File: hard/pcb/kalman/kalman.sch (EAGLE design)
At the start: 89 parts, among them X1 USB-SMD-NS

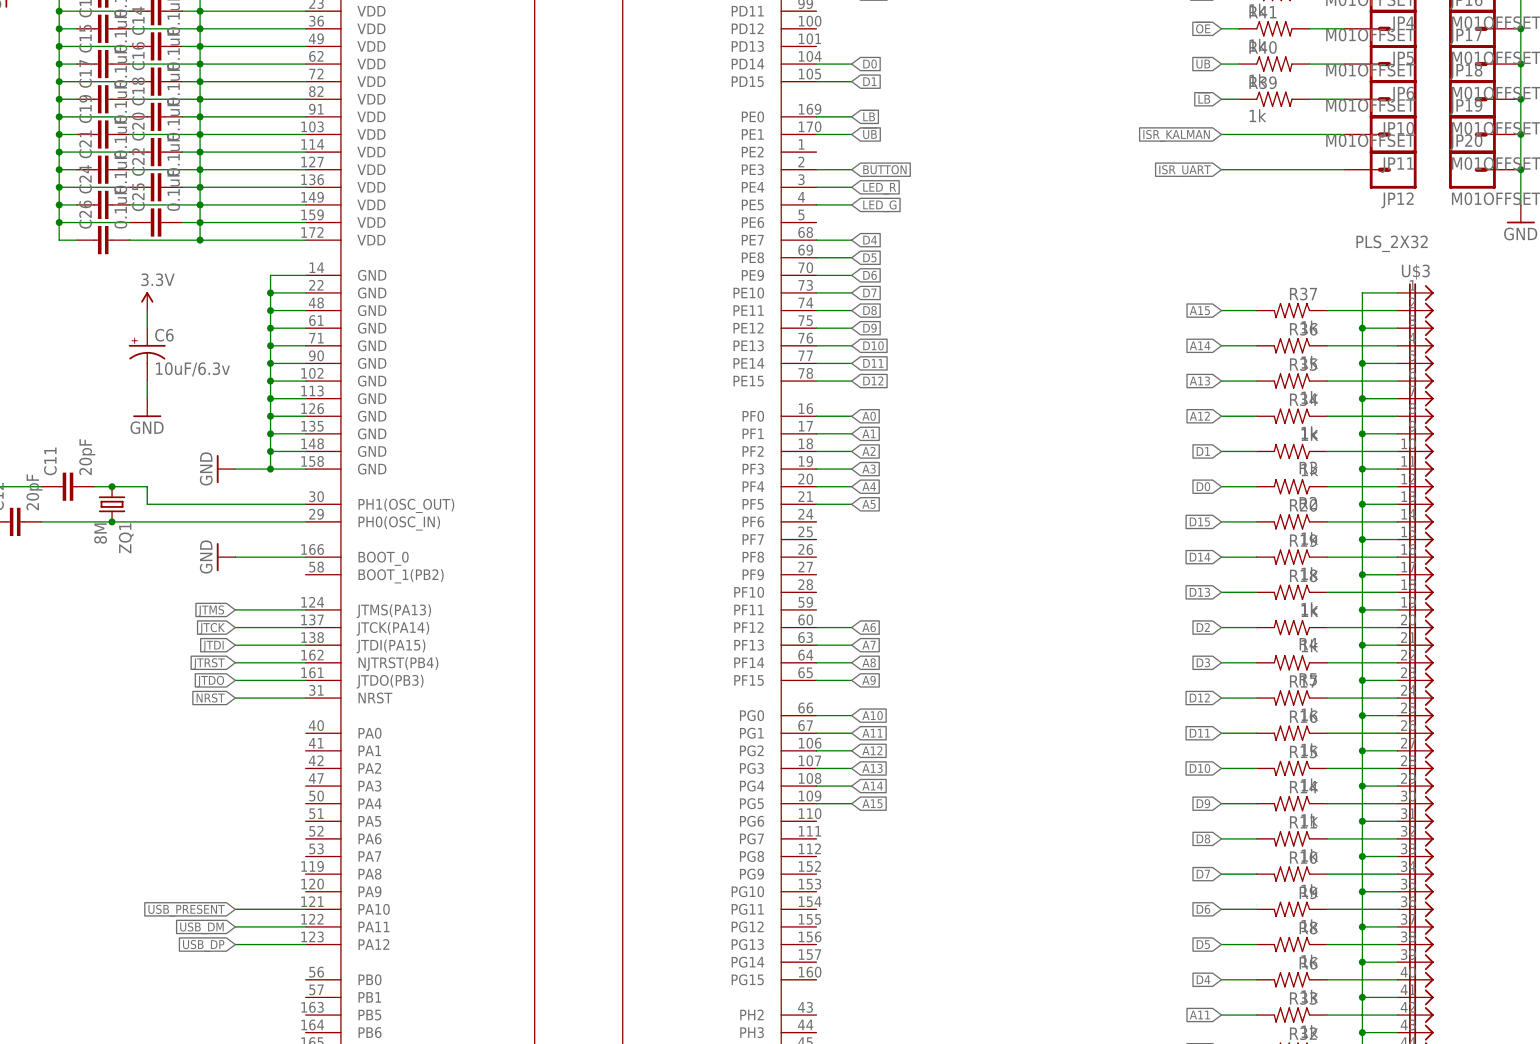
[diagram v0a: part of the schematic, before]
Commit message: updated kalman tester
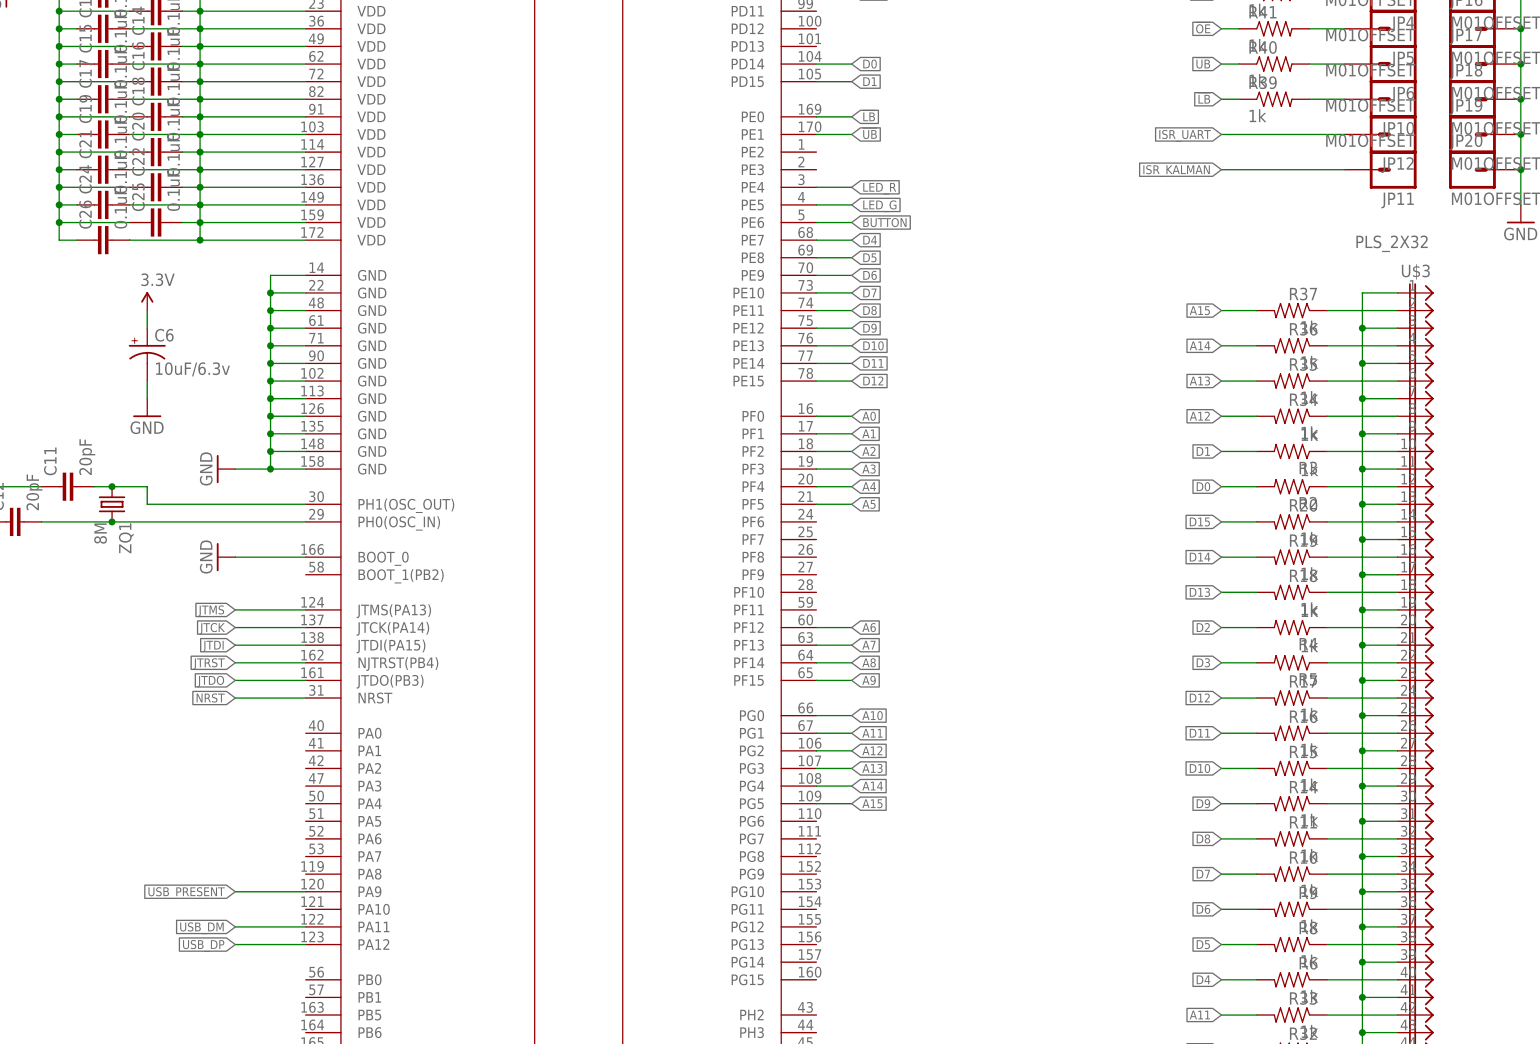
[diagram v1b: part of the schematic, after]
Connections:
- net BUTTON: now also U$4.PE6; no longer U$4.PE3
- net USB_PRESENT: now also U$4.PA9; no longer U$4.PA10
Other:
- moved on the sheet: JP11, JP12
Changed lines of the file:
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@@
 <?xml version="1.0" encoding="utf-8"?>
 <!DOCTYPE eagle SYSTEM "eagle.dtd">
-<eagle version="6.6.0">
+<eagle version="7.2.0">
 <drawing>
 <settings>
@@
 <instance part="JP6" gate="G$1" x="114.3" y="78.74" rot="R180"/>
 <instance part="JP10" gate="G$1" x="114.3" y="73.66" rot="R180"/>
-<instance part="JP11" gate="G$1" x="114.3" y="68.58" rot="R180"/>
-<instance part="JP12" gate="G$1" x="114.3" y="63.5" rot="R180"/>
+<instance part="JP11" gate="G$1" x="114.3" y="63.5" rot="R180"/>
+<instance part="JP12" gate="G$1" x="114.3" y="68.58" rot="R180"/>
 <instance part="JP14" gate="G$1" x="124.46" y="93.98"/>
 <instance part="JP15" gate="G$1" x="124.46" y="88.9"/>
@@
 <segment>
 <label x="35.56" y="58.42" size="1.27" layer="95" xref="yes"/>
+<wire x1="35.56" y1="58.42" x2="30.48" y2="58.42" width="0.1524" layer="91"/>
 <pinref part="U$4" gate="G$1" pin="PE5"/>
-<wire x1="30.48" y1="58.42" x2="35.56" y2="58.42" width="0.1524" layer="91"/>
 </segment>
 </net>
@@
 <segment>
 <label x="35.56" y="60.96" size="1.27" layer="95" xref="yes"/>
+<wire x1="35.56" y1="60.96" x2="30.48" y2="60.96" width="0.1524" layer="91"/>
 <pinref part="U$4" gate="G$1" pin="PE4"/>
-<wire x1="30.48" y1="60.96" x2="35.56" y2="60.96" width="0.1524" layer="91"/>
 </segment>
 </net>
@@
 </segment>
 <segment>
-<pinref part="U$4" gate="G$1" pin="PA10"/>
-<wire x1="-43.18" y1="-43.18" x2="-53.34" y2="-43.18" width="0.1524" layer="91"/>
-<label x="-53.34" y="-43.18" size="1.27" layer="95" rot="R180" xref="yes"/>
+<label x="-53.34" y="-40.64" size="1.27" layer="95" rot="R180" xref="yes"/>
+<pinref part="U$4" gate="G$1" pin="PA9"/>
+<wire x1="-53.34" y1="-40.64" x2="-43.18" y2="-40.64" width="0.1524" layer="91"/>
 </segment>
 </net>
@@
 <segment>
 <pinref part="JP11" gate="G$1" pin="1"/>
-<wire x1="106.68" y1="68.58" x2="88.9" y2="68.58" width="0.1524" layer="91"/>
-<label x="88.9" y="68.58" size="1.27" layer="95" rot="R180" xref="yes"/>
+<wire x1="106.68" y1="63.5" x2="88.9" y2="63.5" width="0.1524" layer="91"/>
+<label x="88.9" y="63.5" size="1.27" layer="95" rot="R180" xref="yes"/>
 </segment>
 <segment>
@@
 <segment>
 <pinref part="JP12" gate="G$1" pin="1"/>
-<wire x1="106.68" y1="63.5" x2="88.9" y2="63.5" width="0.1524" layer="91"/>
-<label x="88.9" y="63.5" size="1.27" layer="95" rot="R180" xref="yes"/>
+<wire x1="106.68" y1="68.58" x2="88.9" y2="68.58" width="0.1524" layer="91"/>
+<label x="88.9" y="68.58" size="1.27" layer="95" rot="R180" xref="yes"/>
 </segment>
 <segment>
@@
 </segment>
 <segment>
-<pinref part="U$4" gate="G$1" pin="PE3"/>
-<wire x1="30.48" y1="63.5" x2="35.56" y2="63.5" width="0.1524" layer="91"/>
-<label x="35.56" y="63.5" size="1.27" layer="95" xref="yes"/>
-</segment>
-</net>
+<label x="35.56" y="55.88" size="1.27" layer="95" xref="yes"/>
+<wire x1="30.48" y1="55.88" x2="35.56" y2="55.88" width="0.1524" layer="91"/>
+<pinref part="U$4" gate="G$1" pin="PE6"/>
+</segment>
+</net>
